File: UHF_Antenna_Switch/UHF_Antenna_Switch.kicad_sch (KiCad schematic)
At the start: 31 parts, among them J1 Conn_N_Type_Female, J2 Conn_SO-239, J3 Conn_SMA_Female, J4 Screw_Terminal_01x04, J5 Conn_02x03_Odd_Even, SW1 SW_SP3T, SW2 SW_Push, U1 LTC5507ES6, U2 PAT1220-C-10DB, U3 PCB-Trace-RF-Coupler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

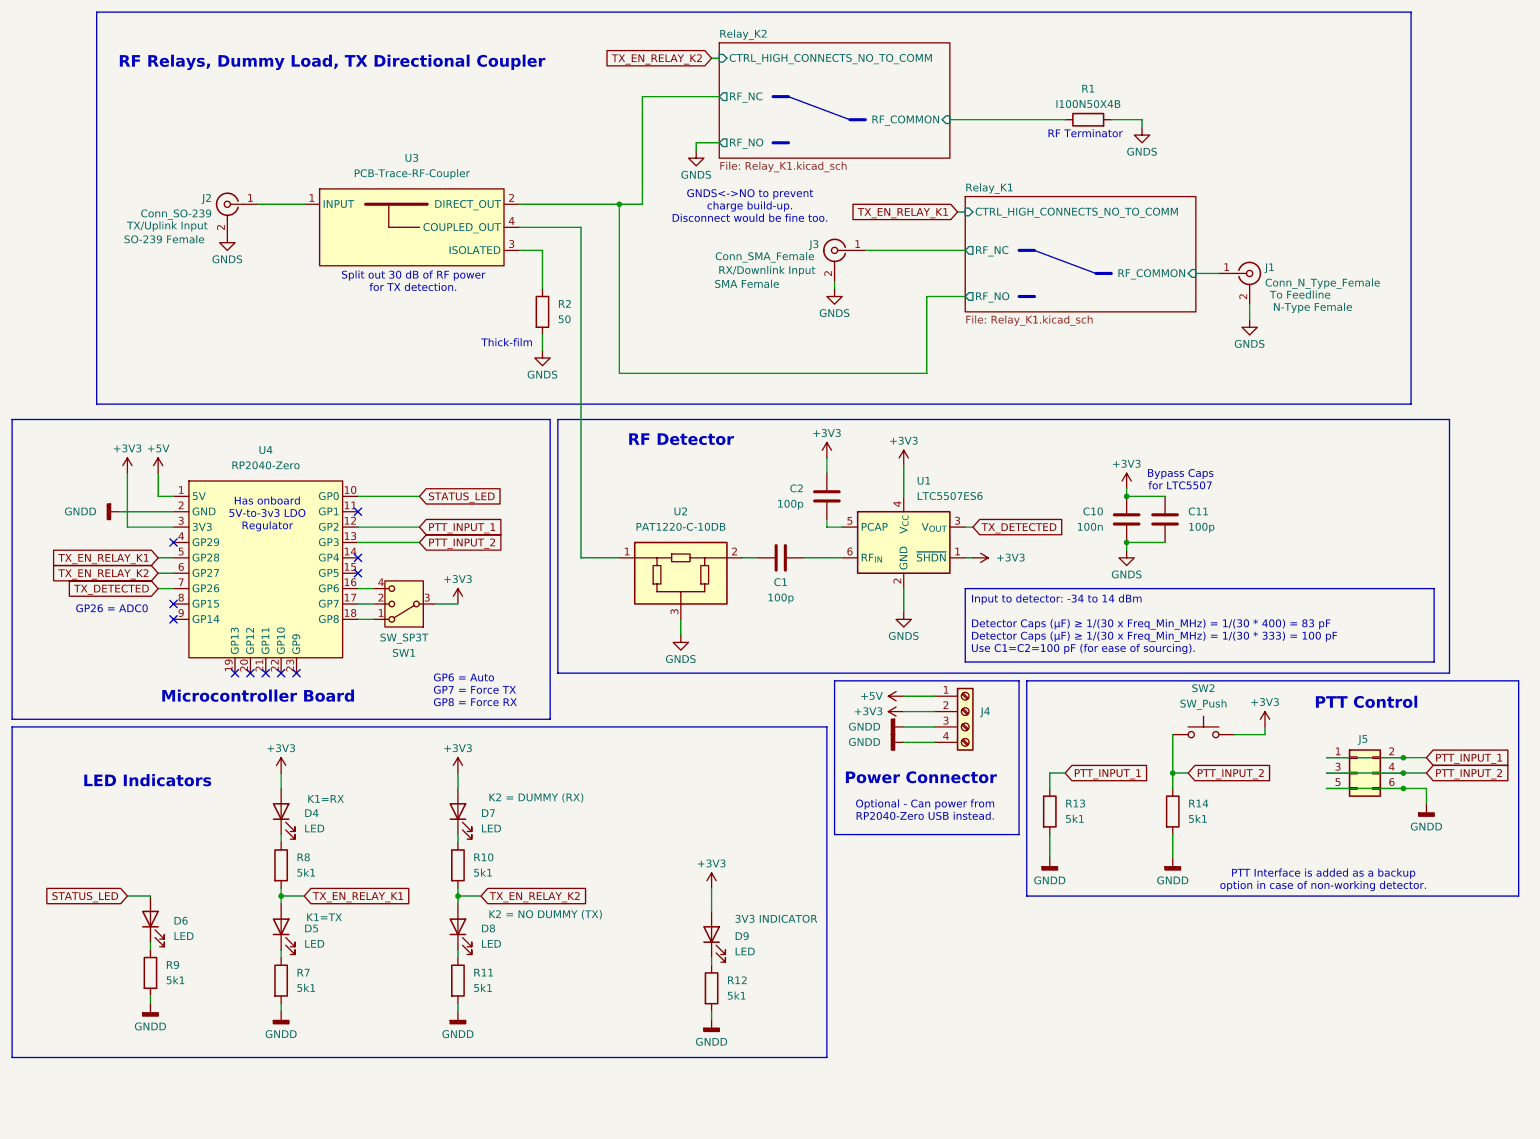
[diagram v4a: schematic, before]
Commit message: PCB: Route digital components
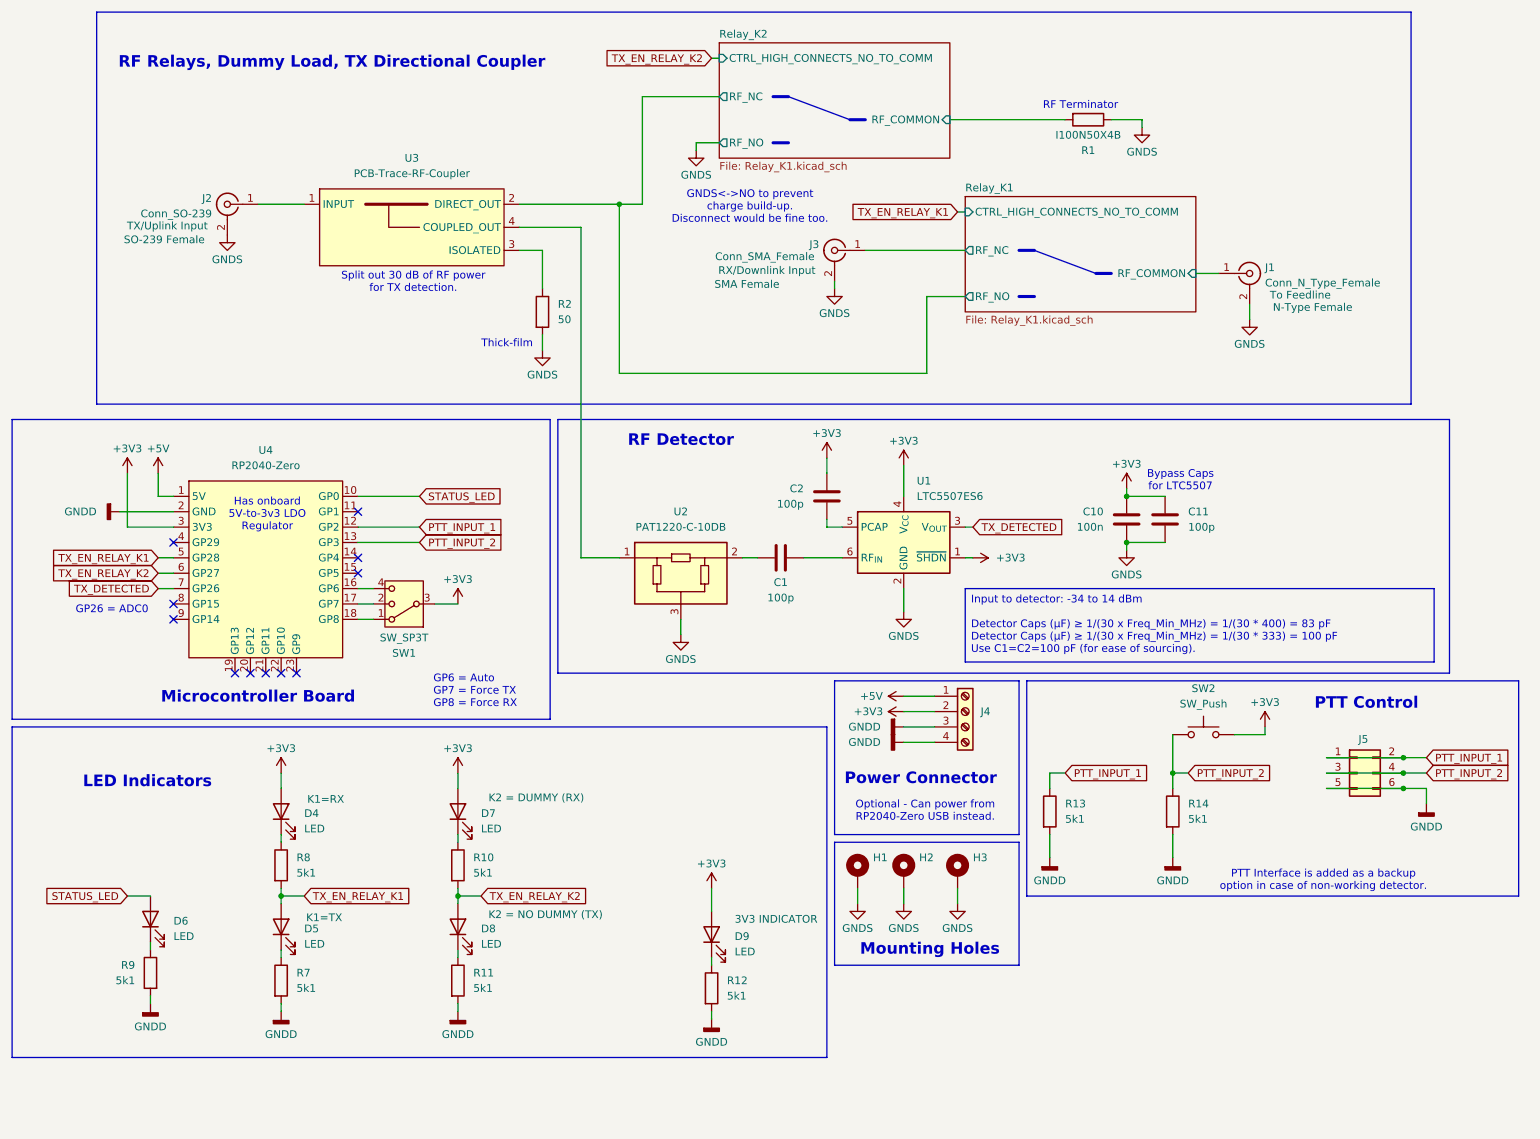
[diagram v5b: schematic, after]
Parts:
- added H1, H2, H3: MountingHole_Pad, MountingHole:MountingHole_3.2mm_M3_Pad, symbol Mechanical:MountingHole_Pad
- J3: footprint Connector_Coaxial:SMA_Amphenol_901-143_Horizontal -> Connector_Coaxial:SMA_Amphenol_901-144_Vertical
- R1: footprint (none) -> 00-project-footprints:I100N50X4B-On-PCB
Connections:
- net GNDS: now also R1.1, H1.1, H2.1, H3.1; no longer R1.2
- net Relay_K2/RF_COMMON: now also R1.2; no longer R1.1
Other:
- note added: "Mounting Holes"
- moved on the sheet: R1

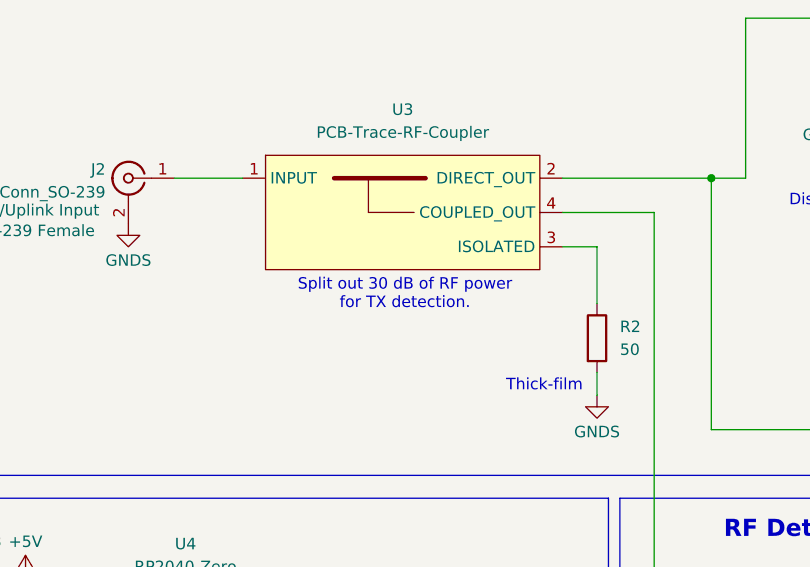
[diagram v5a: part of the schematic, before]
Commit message: PCB: Resolve DRC issues
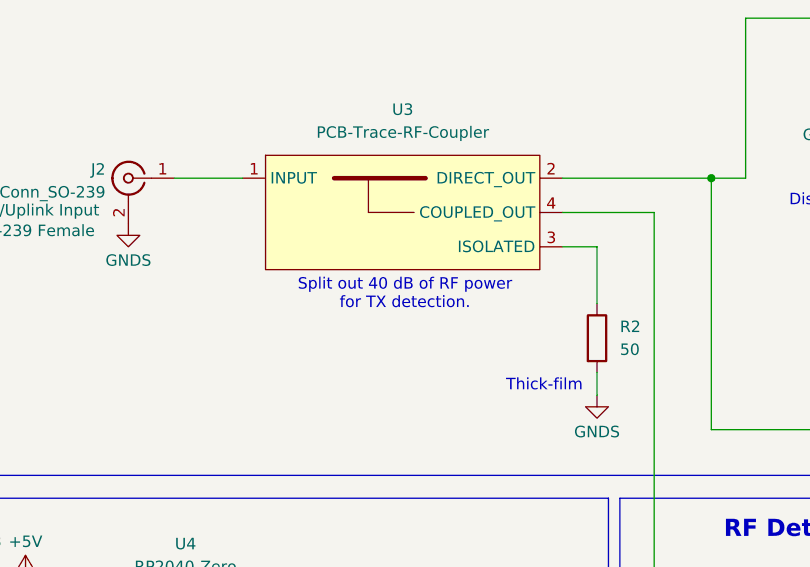
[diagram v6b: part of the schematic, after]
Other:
- note added: "Split out 40 dB of RF power for TX detection."
- note removed: "Split out 30 dB of RF power for TX detection."
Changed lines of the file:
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@@
 		)
 	)
-	(text "Split out 30 dB of RF power\nfor TX detection."
+	(text "Split out 40 dB of RF power\nfor TX detection."
 		(exclude_from_sim no)
 		(at 80.264 58.674 0)

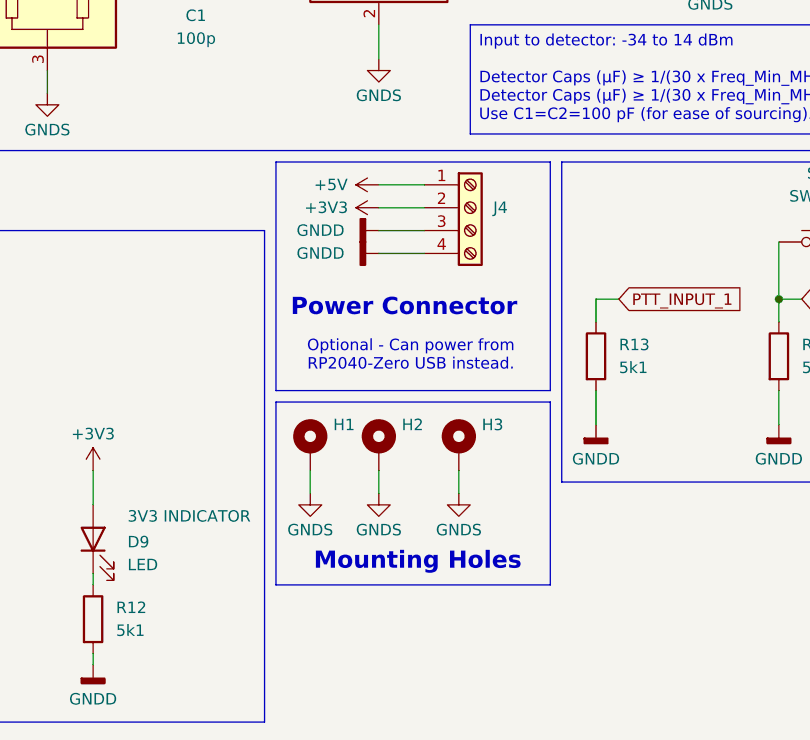
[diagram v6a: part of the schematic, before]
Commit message: PCB: Add 4th mounting hole
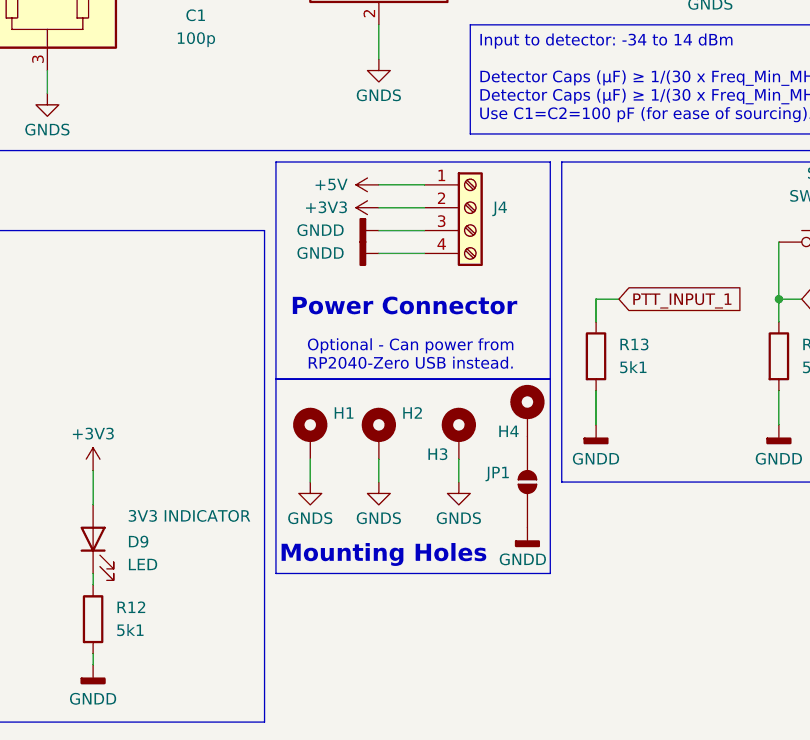
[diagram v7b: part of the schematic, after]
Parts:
- added H4: MountingHole_Pad, MountingHole:MountingHole_3.2mm_M3_Pad, symbol Mechanical:MountingHole_Pad
- added JP1: SolderJumper_2_Open, symbol Jumper:SolderJumper_2_Open
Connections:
- net GNDD: now also JP1.1 (A)
- new net: H4.1, JP1.2 (B)
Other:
- moved on the sheet: H1, H2, H3

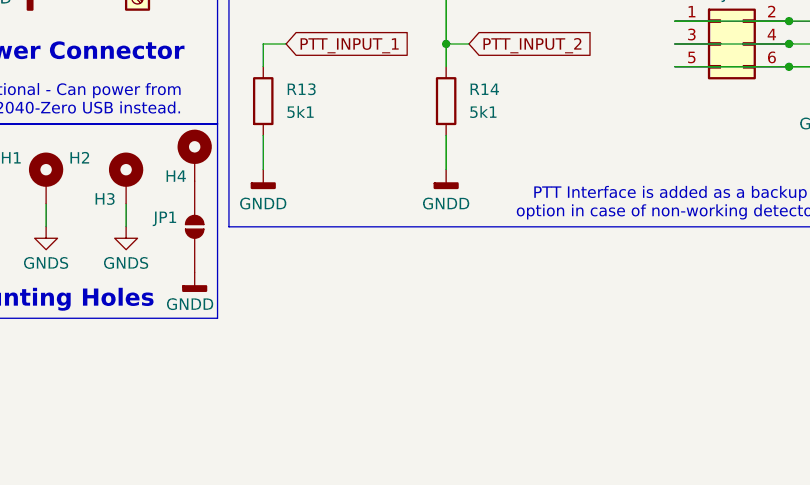
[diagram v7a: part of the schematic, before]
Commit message: Bond RF and Digital GNDs
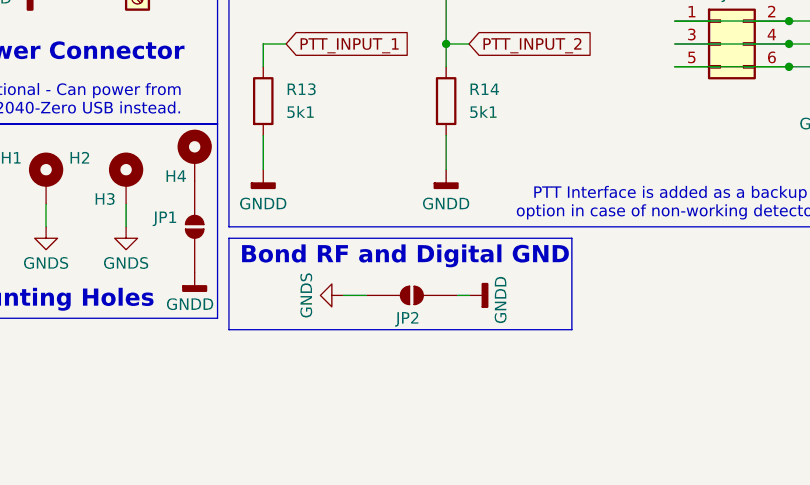
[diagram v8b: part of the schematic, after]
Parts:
- added JP2: SolderJumper_2_Open, Jumper:SolderJumper-2_P1.3mm_Open_RoundedPad1.0x1.5mm, symbol Jumper:SolderJumper_2_Open
- JP1: footprint (none) -> Jumper:SolderJumper-2_P1.3mm_Open_RoundedPad1.0x1.5mm
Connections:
- net GNDD: now also JP2.1 (A)
- net GNDS: now also JP2.2 (B)
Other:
- note added: "Bond RF and Digital GND"
